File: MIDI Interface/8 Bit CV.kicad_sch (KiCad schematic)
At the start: 9 parts, among them U31 LTC1665, U4 TL074, U5 TL074

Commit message: Start MIDI interface board
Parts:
- C1501: renamed from C57; footprint (none) -> 0_Capacitor_THT:C_Disc_D5.5mm_W4.0mm_P2.50mm
- C1502: renamed from C58; footprint (none) -> 0_Capacitor_THT:C_Disc_D5.5mm_W2.5mm_P2.50mm
- C1503: renamed from C59; footprint (none) -> 0_Capacitor_THT:C_Disc_D5.5mm_W2.5mm_P2.50mm
- C1504: renamed from C60; footprint (none) -> 0_Capacitor_THT:C_Disc_D5.5mm_W2.5mm_P2.50mm
- C1505: renamed from C61; footprint (none) -> 0_Capacitor_THT:C_Disc_D5.5mm_W2.5mm_P2.50mm
- C1506: renamed from C62; footprint (none) -> 0_Capacitor_THT:C_Disc_D5.5mm_W2.5mm_P2.50mm
- U1501: renamed from U31; footprint (none) -> Package_DIP:DIP-16_W7.62mm_Socket; symbol Custom:LTC1665 -> 0_Analog_DAC:LTC1665
- U1502: renamed from U4; footprint (none) -> Package_DIP:DIP-14_W7.62mm_Socket
- U1503: renamed from U5; footprint (none) -> Package_DIP:DIP-14_W7.62mm_Socket

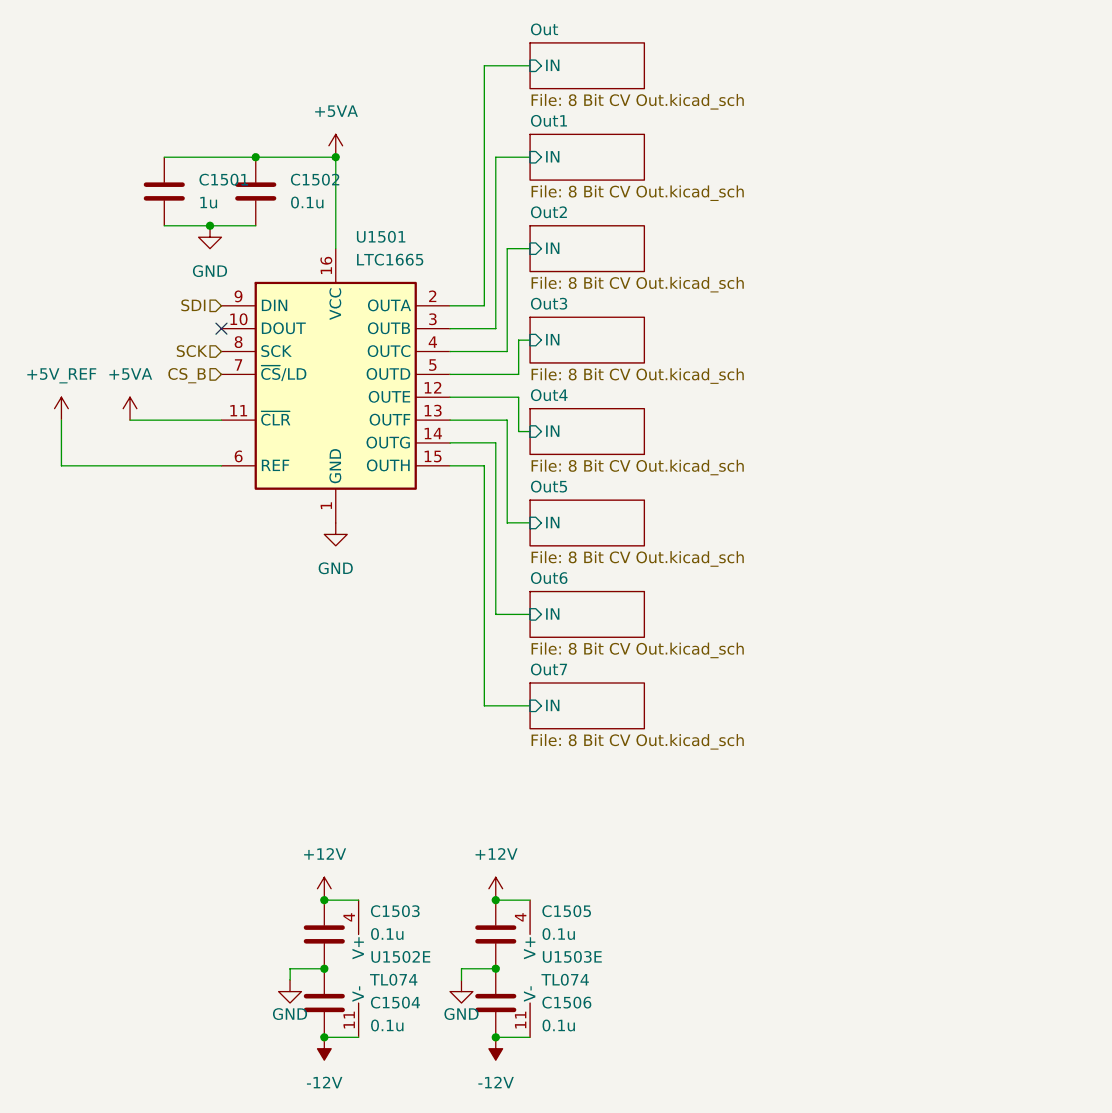
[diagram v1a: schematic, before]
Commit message: New MIDI controller, new envelope generator
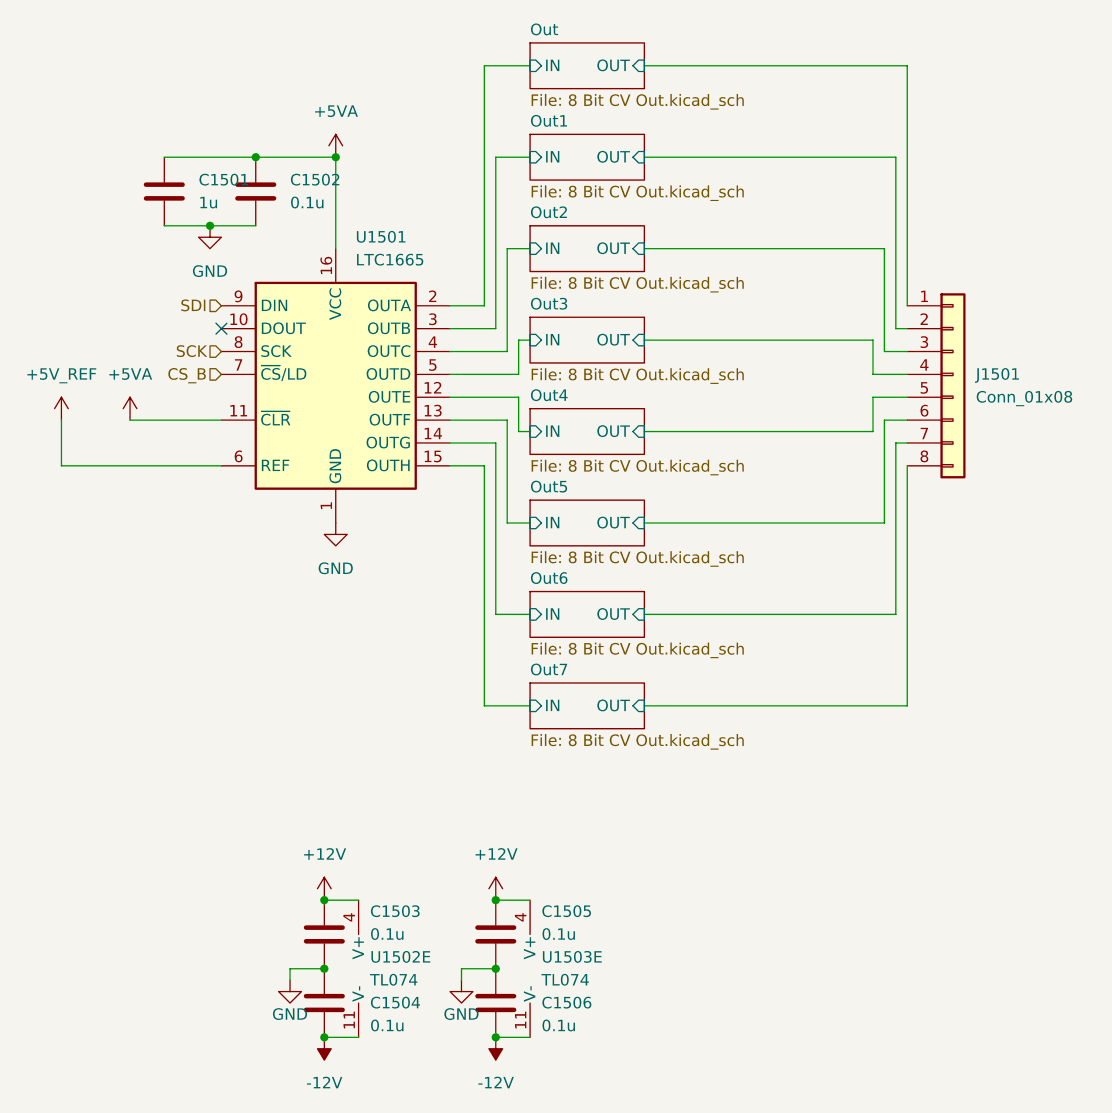
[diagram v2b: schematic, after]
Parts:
- added J1501: Conn_01x08, Connector_PinHeader_2.54mm:PinHeader_1x08_P2.54mm_Vertical, symbol Connector_Generic:Conn_01x08
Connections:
- new net Out/OUT: J1501.1 (Pin_1)
- new net Out1/OUT: J1501.2 (Pin_2)
- new net Out2/OUT: J1501.3 (Pin_3)
- new net Out3/OUT: J1501.4 (Pin_4)
- new net Out4/OUT: J1501.5 (Pin_5)
- new net Out5/OUT: J1501.6 (Pin_6)
- new net Out6/OUT: J1501.7 (Pin_7)
- new net Out7/OUT: J1501.8 (Pin_8)
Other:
- sheet Out ports: added OUT; removed none
- sheet Out1 ports: added OUT; removed none
- sheet Out2 ports: added OUT; removed none
- sheet Out3 ports: added OUT; removed none
- sheet Out4 ports: added OUT; removed none
- sheet Out5 ports: added OUT; removed none
- sheet Out6 ports: added OUT; removed none
- sheet Out7 ports: added OUT; removed none
